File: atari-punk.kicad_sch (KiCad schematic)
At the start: 25 parts, among them J1 Barrel_Jack_Switch, J2 Euro_Power, J3 CV2, J4 CV1, J5 CV4, J6 CV3, J7 AUDIO_OUT, U1 LM555xN, U2 LM555xN

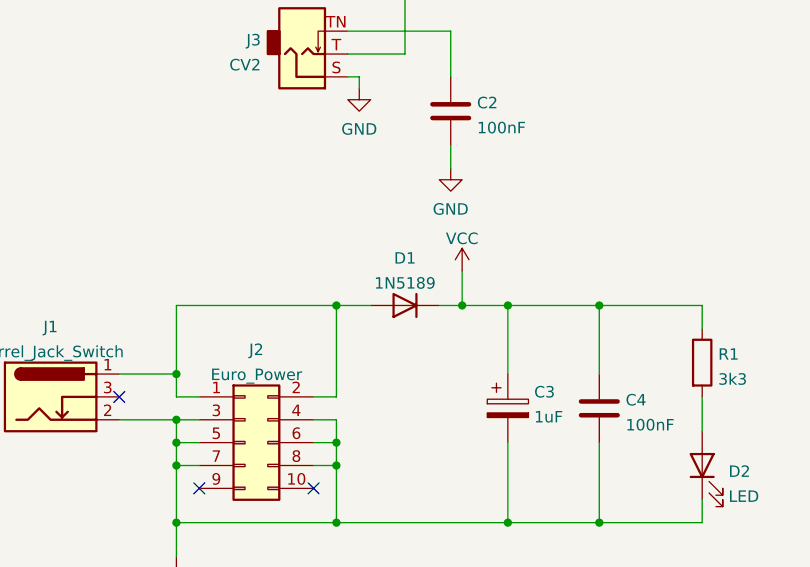
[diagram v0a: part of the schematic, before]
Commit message: Changing diodes
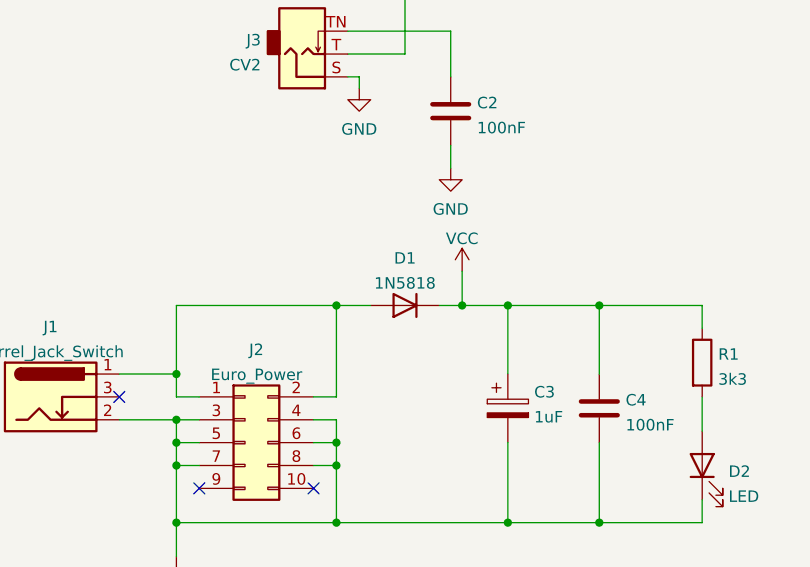
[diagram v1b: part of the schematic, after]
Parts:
- D1: value 1N5189 -> 1N5818
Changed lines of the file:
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@@
     (in_bom yes) (on_board yes) (fields_autoplaced)
     (property "Reference" "D1" (id 0) (at 66.04 131.9235 0))
-    (property "Value" "1N5189" (id 1) (at 66.04 134.6986 0))
+    (property "Value" "1N5818" (id 1) (at 66.04 134.6986 0))
     (property "Footprint" "Rumblesan_Footprints:Diode_THT_P7.62mm_Horizontal" (id 2) (at 66.04 137.16 0)
       (effects (font (size 1.27 1.27)) hide)
@@
     )
     (path "/f693b5bf-7fea-4034-a3f1-b7b48ee22d4f"
-      (reference "D1") (unit 1) (value "1N5189") (footprint "Rumblesan_Footprints:Diode_THT_P7.62mm_Horizontal")
+      (reference "D1") (unit 1) (value "1N5818") (footprint "Rumblesan_Footprints:Diode_THT_P7.62mm_Horizontal")
     )
     (path "/be2d1623-0d0f-4730-b032-0865032586a5"

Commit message: Fixing for rev2
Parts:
- removed J2: Euro_Power, Connector_PinSocket_2.54mm:PinSocket_2x05_P2.54mm_Vertical, symbol Connector_Generic:Conn_02x05_Odd_Even
- removed J4: CV1, AudioJacks:Jack_3.5mm_QingPu_WQP-PJ398SM_Vertical, symbol Connector:AudioJack2_SwitchT
- removed J6: CV3, AudioJacks:Jack_3.5mm_QingPu_WQP-PJ398SM_Vertical, symbol Connector:AudioJack2_SwitchT
- added J2: Eurorack_Power_Small, EurorackBasics:Eurorack_PowerHeader_2x05_P2.54mm_Bare, symbol Eurorack_Hardware:Eurorack_Power_Small
- C1, C2, C4, C5: footprint Rumblesan_Footprints:C_Rect_L7.0mm_W3.5mm_P2.50mm_P5.00mm -> Rumblesan_Footprints:C_Rect_L7.0mm_W3.5mm_P5.00mm
- C6: value 10nF -> 100nF; footprint Rumblesan_Footprints:C_Rect_L7.0mm_W3.5mm_P2.50mm_P5.00mm -> Rumblesan_Footprints:C_Rect_L7.0mm_W3.5mm_P5.00mm
- J1: footprint Connector_BarrelJack:BarrelJack_CUI_PJ-102AH_Horizontal -> Connector_BarrelJack:BarrelJack_GCT_DCJ200-10-A_Horizontal
- J3: value CV2 -> CV1; footprint AudioJacks:Jack_3.5mm_QingPu_WQP-PJ398SM_Vertical -> EurorackBasics:Jack_3.5mm_QingPu_WQP-PJ398SM_Vertical
- J5: value CV4 -> CV2; footprint AudioJacks:Jack_3.5mm_QingPu_WQP-PJ398SM_Vertical -> EurorackBasics:Jack_3.5mm_QingPu_WQP-PJ398SM_Vertical
- J7: footprint AudioJacks:Jack_3.5mm_QingPu_WQP-PJ398SM_Vertical -> EurorackBasics:Jack_3.5mm_QingPu_WQP-PJ398SM_Vertical
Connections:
- net GND: now also J2.3 (GND), J2.4 (GND), J2.5 (GND), J2.6 (GND), J2.7 (GND), J2.8 (GND)
- net at R2.2, U1.7 (DIS): now also RV1.3
- net at C6.1, U2.6 (THR), U2.7 (DIS): now also RV2.3
- net at D1.2 (A), J1.1: now also J2.10 (+12V), J2.9 (+12V)
- new net: J2.1 (-12V), J2.2 (-12V)
- no-connect marks 4 -> 3
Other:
- moved on the sheet: C2, D1, J1, R3, R4, RV1, RV2

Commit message: Updating layout
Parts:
- added H1, H2, H3: MountingHole_Pad, MountingHole:MountingHole_3.2mm_M3_DIN965_Pad, symbol Mechanical:MountingHole_Pad
- C1, C2, C4, C5, C6: footprint Rumblesan_Footprints:C_Rect_L7.0mm_W3.5mm_P5.00mm -> rumblesan-standard-parts:C_Rect_L7.0mm_W3.5mm_P5.00mm
- C3, C7: footprint Rumblesan_Footprints:CP_Radial_D6.3mm_P2.50mm -> rumblesan-standard-parts:CP_Radial_D6.3mm_P2.50mm
- D1: footprint Rumblesan_Footprints:Diode_THT_P7.62mm_Horizontal -> rumblesan-standard-parts:D_DO-35_SOD27_P7.62mm_Horizontal
- J2: footprint EurorackBasics:Eurorack_PowerHeader_2x05_P2.54mm_Bare -> eurorack-power:Eurorack_PowerHeader_2x05_P2.54mm_Bare
- J3, J5, J7: footprint EurorackBasics:Jack_3.5mm_QingPu_WQP-PJ398SM_Vertical -> rumblesan-standard-parts:Jack_3.5mm_QingPu_WQP-PJ398SM_Vertical
- R1, R2, R3, R4: footprint Rumblesan_Footprints:R_Axial_DIN0207_L6.3mm_D2.5mm_P7.62mm_Horizontal -> rumblesan-standard-parts:R_Axial_DIN0207_L6.3mm_D2.5mm_P10.16mm_Horizontal
- RV1, RV2, RV3: footprint Rumblesan_Footprints:Potentiometer_Alpha_RD901F-40-00D_Single_Vertical_CircularHoles -> rumblesan-standard-parts:Potentiometer_Alpha_RD901F-40-00D_Single_Vertical
- U1, U2: footprint Package_DIP:DIP-8_W7.62mm -> rumblesan-standard-parts:DIP-8_W7.62mm_Socket
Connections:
- net GND: now also H1.1, H2.1, H3.1
